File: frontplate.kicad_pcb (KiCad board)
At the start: 2 copper layers, 190.3 x 95 mm, 5 parts

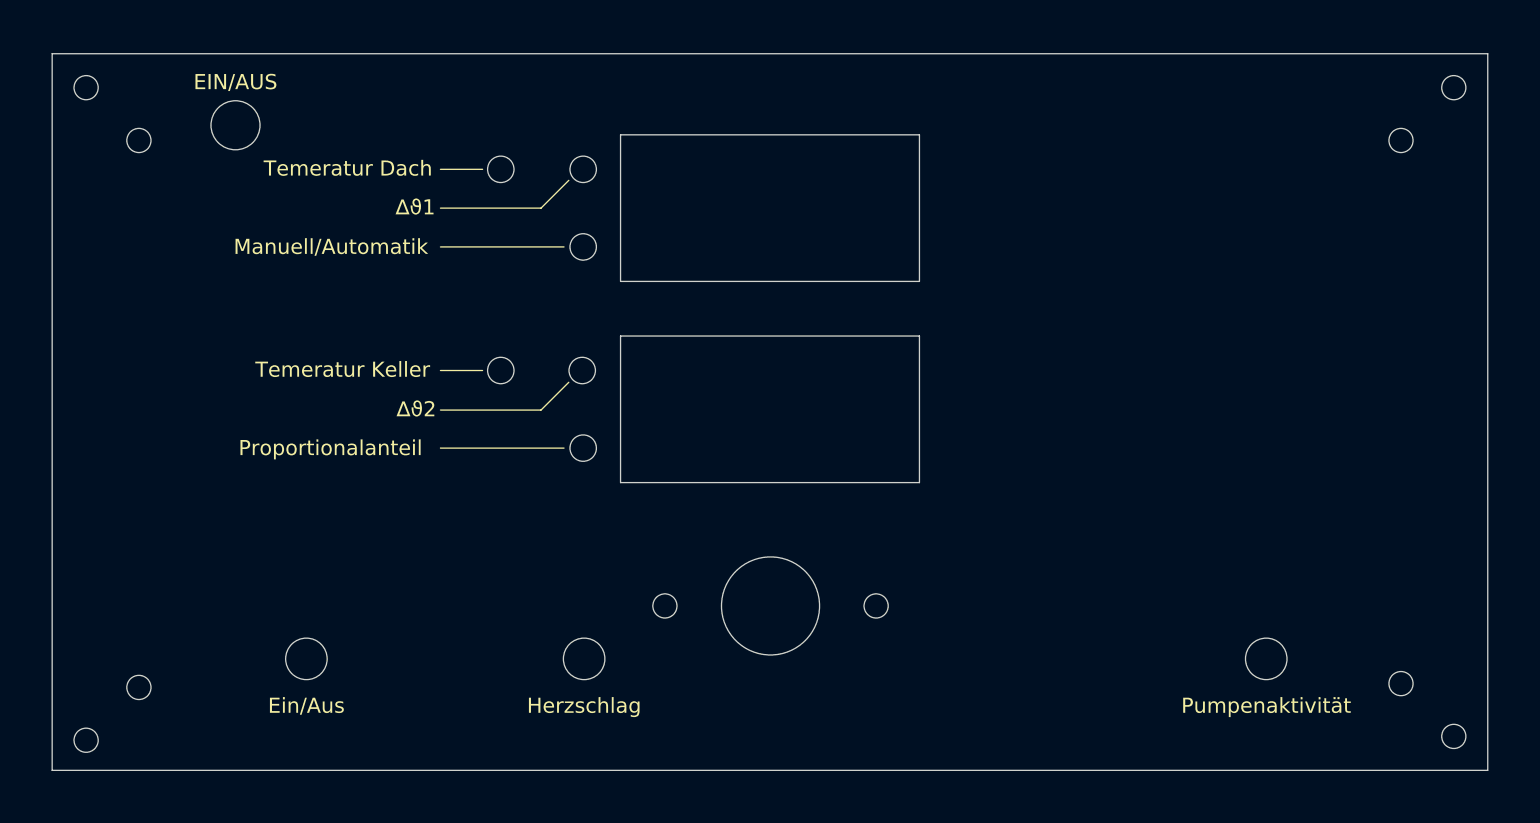
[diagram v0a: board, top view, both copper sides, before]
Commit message: added mcad assembly
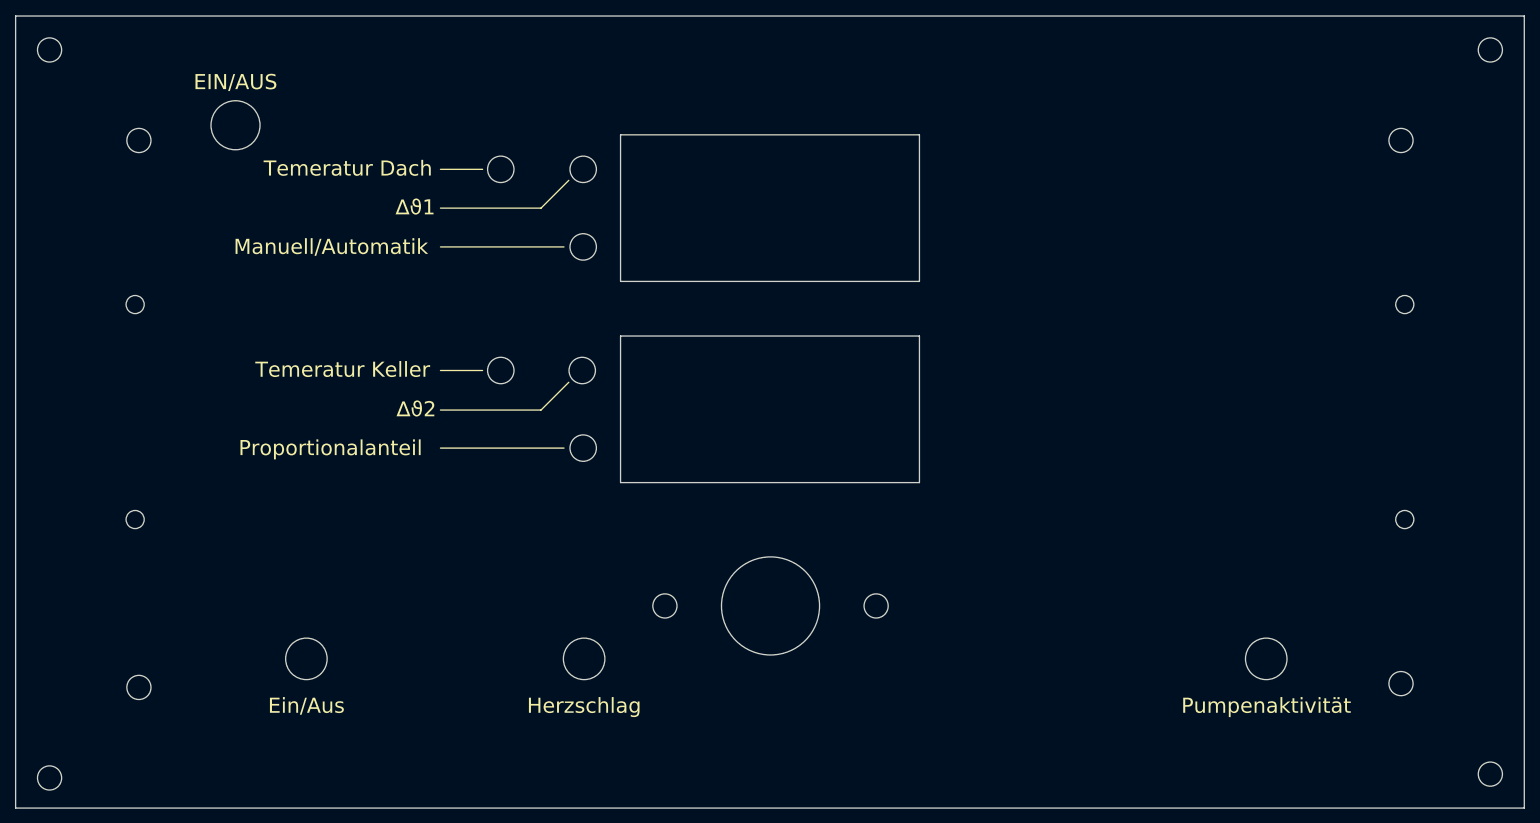
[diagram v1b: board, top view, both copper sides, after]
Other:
- board size 190.3 x 95 mm -> 200 x 105 mm
- board text added: "200mm x 105mm"
- board text added: "Note: Conrad: 183592 - 62 as grips (x2)"
- board text removed: "191mm x 95mm"
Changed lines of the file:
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@@
   (general
     (thickness 1.6)
-    (drawings 52)
+    (drawings 57)
     (tracks 0)
     (zones 0)
@@
   )
   (setup
-    (last_trace_width 1.5)
+    (last_trace_width 0.25)
     (user_trace_width 0.25)
     (user_trace_width 0.5)
@@
   (module dummy:void (layer F.Cu)
     (at 225.631 149.479)
-    (fp_text reference MECH5 (at 9.192 2.159) (layer F.SilkS) hide
+    (fp_text reference MECH5 (at 9.573 7.874) (layer F.SilkS) hide
       (effects (font (size 1 1) (thickness 0.15)))
     )
@@
   (module dummy:void (layer F.Cu)
     (at 224.131 150.979)
-    (fp_text reference MECH4 (at 4.596 0.659) (layer F.SilkS) hide
+    (fp_text reference MECH4 (at 4.469 6.501) (layer F.SilkS) hide
       (effects (font (size 1 1) (thickness 0.15)))
     )
@@
   (module dummy:void (layer F.Cu)
     (at 224.131 149.479)
-    (fp_text reference MECH3 (at 4.596 -0.254) (layer F.SilkS) hide
+    (fp_text reference MECH3 (at 4.342 5.715) (layer F.SilkS) hide
       (effects (font (size 1 1) (thickness 0.15)))
     )
@@
   (module dummy:void (layer F.Cu)
     (at 222.631 150.979)
-    (fp_text reference MECH2 (at 0 0.5) (layer F.SilkS) hide
+    (fp_text reference MECH2 (at -0.254 6.628) (layer F.SilkS) hide
       (effects (font (size 1 1) (thickness 0.15)))
     )
@@
   (module dummy:void (layer F.Cu)
     (at 222.631 149.479)
-    (fp_text reference MECH1 (at 0 -0.254) (layer F.SilkS) hide
+    (fp_text reference MECH1 (at -0.127 5.842) (layer F.SilkS) hide
       (effects (font (size 1 1) (thickness 0.15)))
     )
@@
     )
   )
-  (gr_circle (center 229.588 140.708) (end 231.188 140.708) (layer Edge.Cuts) (width 0.12))
+  (gr_text "Note: Conrad: 183592 - 62 as grips (x2)" (at 86.106 166.751) (layer Eco2.User)
+    (effects (font (size 3 3) (thickness 0.15)))
+  )
+  (gr_circle (center 223.088 111.958) (end 224.288 111.958) (layer Edge.Cuts) (width 0.05))
+  (gr_circle (center 223.088 83.458) (end 224.288 83.458) (layer Edge.Cuts) (width 0.05))
+  (gr_circle (center 54.778 111.958) (end 55.978 111.958) (layer Edge.Cuts) (width 0.05))
+  (gr_circle (center 54.778 83.458) (end 55.978 83.458) (layer Edge.Cuts) (width 0.05))
+  (gr_circle (center 234.433 145.708) (end 236.033 145.708) (layer Edge.Cuts) (width 0.12))
   (gr_circle (center 222.588 133.708) (end 224.188 133.708) (layer Edge.Cuts) (width 0.12))
   (gr_circle (center 153.008 123.413) (end 154.608 123.413) (layer Edge.Cuts) (width 0.12))
   (gr_circle (center 125.008 123.413) (end 126.608 123.413) (layer Edge.Cuts) (width 0.12))
-  (gr_circle (center 229.588 54.708) (end 231.188 54.708) (layer Edge.Cuts) (width 0.12))
+  (gr_circle (center 234.433 49.708) (end 236.033 49.708) (layer Edge.Cuts) (width 0.12))
   (gr_circle (center 222.588 61.708) (end 224.188 61.708) (layer Edge.Cuts) (width 0.12))
-  (gr_circle (center 48.278 141.216) (end 49.878 141.216) (layer Edge.Cuts) (width 0.12))
+  (gr_circle (center 43.433 146.216) (end 45.033 146.216) (layer Edge.Cuts) (width 0.12))
   (gr_circle (center 55.278 134.216) (end 56.878 134.216) (layer Edge.Cuts) (width 0.12))
-  (gr_circle (center 48.278 54.708) (end 49.878 54.708) (layer Edge.Cuts) (width 0.12))
+  (gr_circle (center 43.433 49.708) (end 45.033 49.708) (layer Edge.Cuts) (width 0.12))
   (gr_circle (center 55.278 61.708) (end 56.878 61.708) (layer Edge.Cuts) (width 0.12))
   (gr_text Manuell/Automatik (at 80.724572 75.819) (layer F.SilkS)
@@
   (gr_circle (center 114.173 102.489) (end 115.923 102.489) (layer Edge.Cuts) (width 0.05))
   (gr_circle (center 139.008 123.413) (end 145.508 123.413) (layer Edge.Cuts) (width 0.05))
-  (gr_line (start 43.778 50.208) (end 234.088 50.208) (layer Edge.Cuts) (width 0.05))
-  (gr_text "191mm x 95mm" (at 61.722 152.019) (layer Eco2.User)
+  (gr_line (start 38.933 45.208) (end 238.933 45.208) (layer Edge.Cuts) (width 0.05))
+  (gr_text "200mm x 105mm" (at 57.531 160.147) (layer Eco2.User)
     (effects (font (size 4 3) (thickness 0.3)))
   )
-  (gr_line (start 43.778 145.208) (end 43.778 50.208) (layer Edge.Cuts) (width 0.05))
-  (gr_line (start 234.088 145.208) (end 43.778 145.208) (layer Edge.Cuts) (width 0.05))
-  (gr_line (start 234.088 50.208) (end 234.088 145.208) (layer Edge.Cuts) (width 0.05))
+  (gr_line (start 38.933 150.208) (end 38.933 45.208) (layer Edge.Cuts) (width 0.05))
+  (gr_line (start 238.933 150.208) (end 38.933 150.208) (layer Edge.Cuts) (width 0.05))
+  (gr_line (start 238.933 45.208) (end 238.933 150.208) (layer Edge.Cuts) (width 0.05))
 )

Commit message: some cleaning
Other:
- outline, holes or cut-outs redrawn
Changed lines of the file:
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@@
   (gr_circle (center 114.046 92.202) (end 115.796 92.202) (layer Edge.Cuts) (width 0.05))
   (gr_circle (center 114.173 102.489) (end 115.923 102.489) (layer Edge.Cuts) (width 0.05))
-  (gr_circle (center 139.008 123.413) (end 145.508 123.413) (layer Edge.Cuts) (width 0.05))
+  (gr_circle (center 139.008 123.413) (end 146.008 123.413) (layer Edge.Cuts) (width 0.05))
   (gr_line (start 38.933 45.208) (end 238.933 45.208) (layer Edge.Cuts) (width 0.05))
   (gr_text "200mm x 105mm" (at 57.531 160.147) (layer Eco2.User)

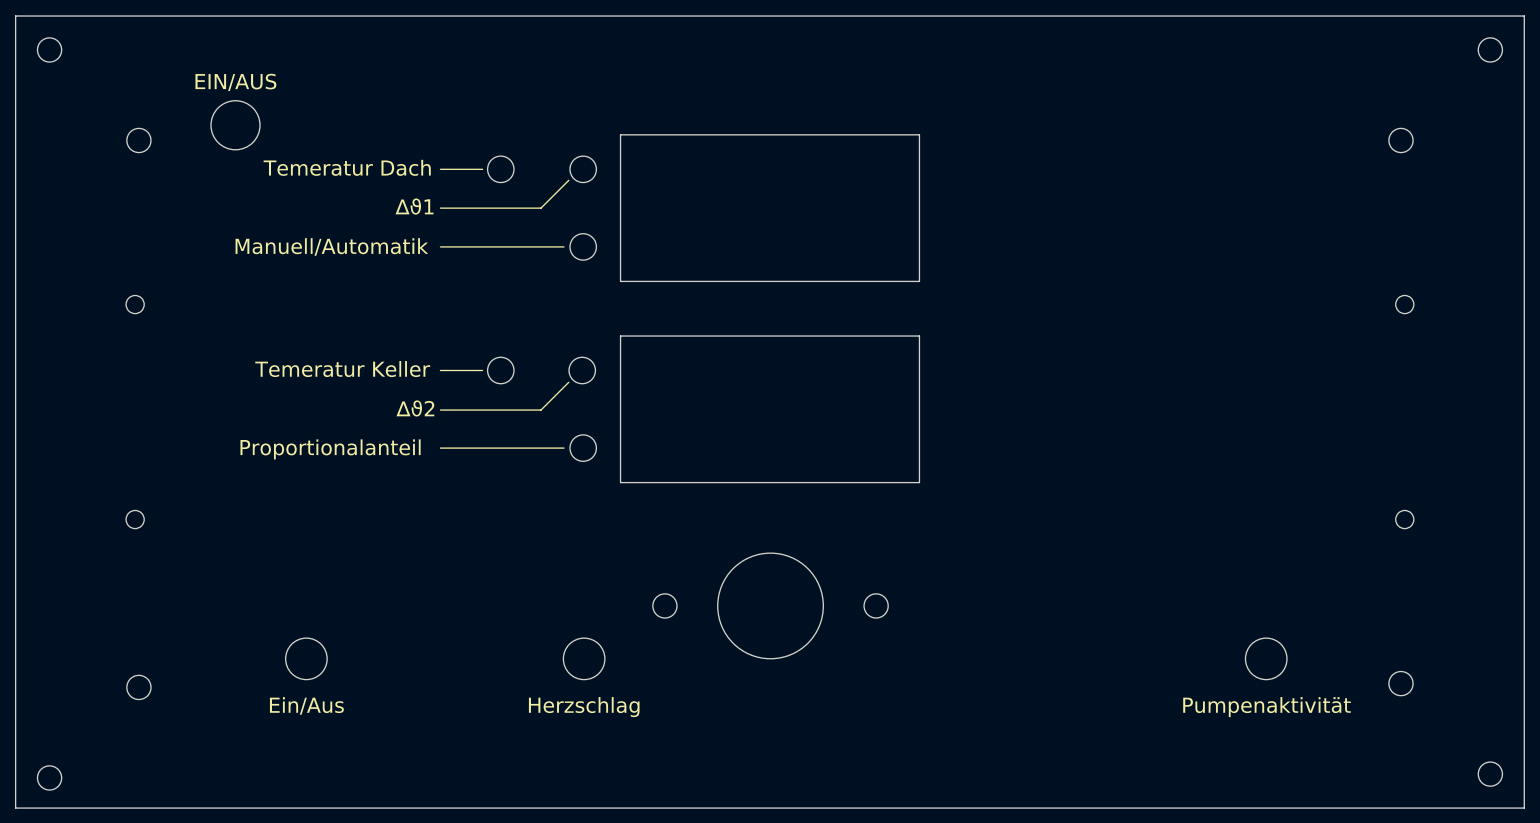
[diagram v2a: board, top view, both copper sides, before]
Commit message: rounded up corners of cutout for display in the frontplate
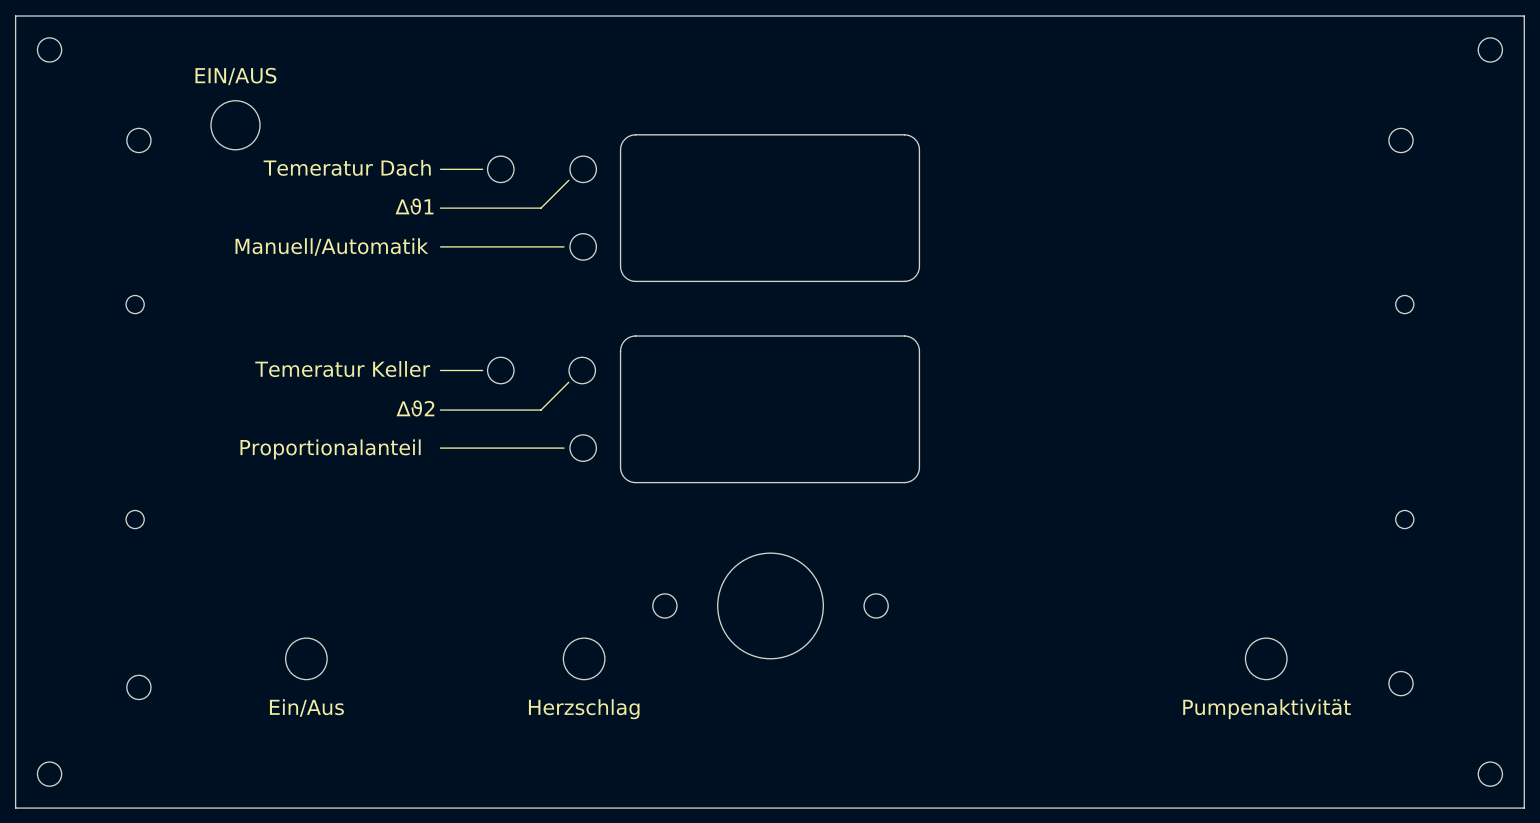
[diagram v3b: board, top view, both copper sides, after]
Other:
- outline, holes or cut-outs redrawn
- board text added: "Note: Conrad: 183592-62 as grips (x2)"
- board text removed: "Note: Conrad: 183592 - 62 as grips (x2)"
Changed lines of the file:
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@@
   (general
     (thickness 1.6)
-    (drawings 57)
+    (drawings 65)
     (tracks 0)
     (zones 0)
@@
   )
   (setup
-    (last_trace_width 0.25)
+    (last_trace_width 1.5)
     (user_trace_width 0.25)
     (user_trace_width 0.5)
@@
     )
   )
-  (gr_text "Note: Conrad: 183592 - 62 as grips (x2)" (at 86.106 166.751) (layer Eco2.User)
+  (gr_arc (start 156.75 105.061) (end 156.75 107.061) (angle -90) (layer Edge.Cuts) (width 0.05))
+  (gr_arc (start 121.126 105.061) (end 119.126 105.061) (angle -90) (layer Edge.Cuts) (width 0.05))
+  (gr_arc (start 156.75 89.63) (end 158.75 89.63) (angle -90) (layer Edge.Cuts) (width 0.05))
+  (gr_arc (start 121.126 89.63) (end 121.126 87.63) (angle -93.6) (layer Edge.Cuts) (width 0.05))
+  (gr_arc (start 156.75 78.391) (end 156.75 80.391) (angle -90) (layer Edge.Cuts) (width 0.05))
+  (gr_arc (start 121.126 78.391) (end 119.126 78.391) (angle -90) (layer Edge.Cuts) (width 0.05))
+  (gr_arc (start 156.75 62.96) (end 158.75 62.96) (angle -90) (layer Edge.Cuts) (width 0.05))
+  (gr_arc (start 121.126 62.96) (end 119.126 62.96) (angle 90) (layer Edge.Cuts) (width 0.05))
+  (gr_text "Note: Conrad: 183592-62 as grips (x2)" (at 86.106 166.751) (layer Eco2.User)
     (effects (font (size 3 3) (thickness 0.15)))
   )
@@
   (gr_circle (center 54.778 111.958) (end 55.978 111.958) (layer Edge.Cuts) (width 0.05))
   (gr_circle (center 54.778 83.458) (end 55.978 83.458) (layer Edge.Cuts) (width 0.05))
-  (gr_circle (center 234.433 145.708) (end 236.033 145.708) (layer Edge.Cuts) (width 0.12))
-  (gr_circle (center 222.588 133.708) (end 224.188 133.708) (layer Edge.Cuts) (width 0.12))
-  (gr_circle (center 153.008 123.413) (end 154.608 123.413) (layer Edge.Cuts) (width 0.12))
-  (gr_circle (center 125.008 123.413) (end 126.608 123.413) (layer Edge.Cuts) (width 0.12))
-  (gr_circle (center 234.433 49.708) (end 236.033 49.708) (layer Edge.Cuts) (width 0.12))
-  (gr_circle (center 222.588 61.708) (end 224.188 61.708) (layer Edge.Cuts) (width 0.12))
-  (gr_circle (center 43.433 146.216) (end 45.033 146.216) (layer Edge.Cuts) (width 0.12))
-  (gr_circle (center 55.278 134.216) (end 56.878 134.216) (layer Edge.Cuts) (width 0.12))
-  (gr_circle (center 43.433 49.708) (end 45.033 49.708) (layer Edge.Cuts) (width 0.12))
-  (gr_circle (center 55.278 61.708) (end 56.878 61.708) (layer Edge.Cuts) (width 0.12))
+  (gr_circle (center 234.433 145.708) (end 236.033 145.708) (layer Edge.Cuts) (width 0.05))
+  (gr_circle (center 222.588 133.708) (end 224.188 133.708) (layer Edge.Cuts) (width 0.05))
+  (gr_circle (center 153.008 123.413) (end 154.608 123.413) (layer Edge.Cuts) (width 0.05))
+  (gr_circle (center 125.008 123.413) (end 126.608 123.413) (layer Edge.Cuts) (width 0.05))
+  (gr_circle (center 234.433 49.708) (end 236.033 49.708) (layer Edge.Cuts) (width 0.05))
+  (gr_circle (center 222.588 61.708) (end 224.188 61.708) (layer Edge.Cuts) (width 0.05))
+  (gr_circle (center 43.433 145.708) (end 45.033 145.708) (layer Edge.Cuts) (width 0.05))
+  (gr_circle (center 55.278 134.216) (end 56.878 134.216) (layer Edge.Cuts) (width 0.05))
+  (gr_circle (center 43.433 49.708) (end 45.033 49.708) (layer Edge.Cuts) (width 0.05))
+  (gr_circle (center 55.278 61.708) (end 56.878 61.708) (layer Edge.Cuts) (width 0.05))
   (gr_text Manuell/Automatik (at 80.724572 75.819) (layer F.SilkS)
     (effects (font (size 2 2) (thickness 0.15)))
@@
   (gr_line (start 95.25 70.6755) (end 108.585 70.6755) (layer F.SilkS) (width 0.12))
   (gr_line (start 95.25 65.532) (end 100.838 65.532) (layer F.SilkS) (width 0.12))
-  (gr_text EIN/AUS (at 68.082 53.975) (layer F.SilkS)
+  (gr_text EIN/AUS (at 68.082 53.19) (layer F.SilkS)
     (effects (font (size 2 2) (thickness 0.15)))
   )
@@
     (effects (font (size 2 2) (thickness 0.15)))
   )
-  (gr_text Ein/Aus (at 77.48 136.652) (layer F.SilkS)
-    (effects (font (size 2 2) (thickness 0.15)))
-  )
-  (gr_text Herzschlag (at 114.3 136.652) (layer F.SilkS)
-    (effects (font (size 2 2) (thickness 0.15)))
-  )
-  (gr_text Pumpenaktivität (at 204.724 136.652) (layer F.SilkS)
-    (effects (font (size 2 2) (thickness 0.15)))
-  )
-  (gr_line (start 158.75 107.061) (end 119.126 107.061) (layer Edge.Cuts) (width 0.05))
-  (gr_line (start 119.126 87.63) (end 158.75 87.63) (layer Edge.Cuts) (width 0.05))
-  (gr_line (start 158.75 87.63) (end 158.75 107.061) (layer Edge.Cuts) (width 0.05))
-  (gr_line (start 119.126 107.061) (end 119.126 87.63) (layer Edge.Cuts) (width 0.05))
-  (gr_line (start 119.126 80.391) (end 119.126 60.96) (layer Edge.Cuts) (width 0.05))
-  (gr_line (start 158.75 80.391) (end 119.126 80.391) (layer Edge.Cuts) (width 0.05))
-  (gr_line (start 158.75 60.96) (end 158.75 80.391) (layer Edge.Cuts) (width 0.05))
-  (gr_line (start 119.126 60.96) (end 158.75 60.96) (layer Edge.Cuts) (width 0.05))
+  (gr_text Ein/Aus (at 77.48 136.929) (layer F.SilkS)
+    (effects (font (size 2 2) (thickness 0.15)))
+  )
+  (gr_text Herzschlag (at 114.3 136.929) (layer F.SilkS)
+    (effects (font (size 2 2) (thickness 0.15)))
+  )
+  (gr_text Pumpenaktivität (at 204.724 136.929) (layer F.SilkS)
+    (effects (font (size 2 2) (thickness 0.15)))
+  )
+  (gr_line (start 156.75 107.061) (end 121.126 107.061) (layer Edge.Cuts) (width 0.05))
+  (gr_line (start 121.126 87.63) (end 156.75 87.63) (layer Edge.Cuts) (width 0.05))
+  (gr_line (start 158.75 89.63) (end 158.75 105.061) (layer Edge.Cuts) (width 0.05))
+  (gr_line (start 119.126 105.061) (end 119.126 89.63) (layer Edge.Cuts) (width 0.05))
+  (gr_line (start 119.126 78.391) (end 119.126 62.96) (layer Edge.Cuts) (width 0.05))
+  (gr_line (start 156.75 80.391) (end 121.126 80.391) (layer Edge.Cuts) (width 0.05))
+  (gr_line (start 158.75 62.96) (end 158.75 78.391) (layer Edge.Cuts) (width 0.05))
+  (gr_line (start 121.126 60.96) (end 156.75 60.96) (layer Edge.Cuts) (width 0.05))
   (gr_circle (center 68.082 59.69) (end 71.332 59.69) (layer Edge.Cuts) (width 0.05))
   (gr_circle (center 77.48 130.429) (end 80.23 130.429) (layer Edge.Cuts) (width 0.05))
@@
   (gr_circle (center 139.008 123.413) (end 146.008 123.413) (layer Edge.Cuts) (width 0.05))
   (gr_line (start 38.933 45.208) (end 238.933 45.208) (layer Edge.Cuts) (width 0.05))
-  (gr_text "200mm x 105mm" (at 57.531 160.147) (layer Eco2.User)
+  (gr_text "200mm x 105mm" (at 60.071 159.639) (layer Eco2.User)
     (effects (font (size 4 3) (thickness 0.3)))
   )
